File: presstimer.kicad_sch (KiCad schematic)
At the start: 31 parts, among them J1 Screw_Terminal_01x02, Q1 NPN, Q2 NPN, SW1 SW_Push, SW2 SW_Push, U1 AP7361C-33ER, U2 ESP32-S3-WROOM-1

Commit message: parts assigned, footprints checked
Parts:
- R1, R2: LCSC (none) -> C99782
- R13: LCSC (none) -> C105881
- R14: LCSC (none) -> C116677
- R3: LCSC (none) -> C22548
- R4: LCSC (none) -> C17477
- SW1, SW2: LCSC (none) -> C720477
- U1: LCSC (none) -> C3743528
- U2: LCSC (none) -> C2913202
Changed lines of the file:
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@@
 			)
 		)
+		(property "LCSC" "C99782"
+			(at 68.58 134.62 0)
+			(hide yes)
+			(show_name no)
+			(do_not_autoplace no)
+			(effects
+				(font
+					(size 1.27 1.27)
+				)
+			)
+		)
 		(pin "2"
 		)
@@
 		(property "LCSC" "C77049"
 			(at 186.69 63.4999 0)
+			(hide yes)
+			(show_name no)
+			(do_not_autoplace no)
 			(effects
 				(font
 					(size 1.27 1.27)
 				)
-				(hide yes)
 			)
 		)
@@
 		(property "LCSC" "C28323"
 			(at 54.61 33.0199 0)
+			(hide yes)
+			(show_name no)
+			(do_not_autoplace no)
 			(effects
 				(font
 					(size 1.27 1.27)
 				)
-				(hide yes)
 			)
 		)
@@
 			)
 		)
+		(property "LCSC" "C720477"
+			(at 161.29 125.73 0)
+			(hide yes)
+			(show_name no)
+			(do_not_autoplace no)
+			(effects
+				(font
+					(size 1.27 1.27)
+				)
+			)
+		)
 		(pin "2"
 		)
@@
 			)
 		)
+		(property "LCSC" "C105881"
+			(at 137.16 163.83 0)
+			(hide yes)
+			(show_name no)
+			(do_not_autoplace no)
+			(effects
+				(font
+					(size 1.27 1.27)
+				)
+			)
+		)
 		(pin "2"
 		)
@@
 		(property "LCSC" "C28326707"
 			(at 44.45 20.32 0)
+			(hide yes)
+			(show_name no)
+			(do_not_autoplace no)
 			(effects
 				(font
 					(size 1.27 1.27)
 				)
-				(hide yes)
 			)
 		)
@@
 			)
 		)
+		(property "LCSC" "C720477"
+			(at 124.46 125.73 0)
+			(hide yes)
+			(show_name no)
+			(do_not_autoplace no)
+			(effects
+				(font
+					(size 1.27 1.27)
+				)
+			)
+		)
 		(pin "2"
 		)
@@
 			)
 		)
+		(property "LCSC" "C22548"
+			(at 95.25 33.0199 0)
+			(hide yes)
+			(show_name no)
+			(do_not_autoplace no)
+			(effects
+				(font
+					(size 1.27 1.27)
+				)
+			)
+		)
 		(pin "2"
 		)
@@
 			)
 		)
+		(property "LCSC" "C17477"
+			(at 124.46 163.83 0)
+			(hide yes)
+			(show_name no)
+			(do_not_autoplace no)
+			(effects
+				(font
+					(size 1.27 1.27)
+				)
+			)
+		)
 		(pin "2"
 		)
@@
 			)
 		)
+		(property "LCSC" "C2913202"
+			(at 228.2033 54.61 0)
+			(hide yes)
+			(show_name no)
+			(do_not_autoplace no)
+			(effects
+				(font
+					(size 1.27 1.27)
+				)
+			)
+		)
 		(pin "7"
 		)
@@
 			)
 		)
+		(property "LCSC" "C99782"
+			(at 68.58 152.4 0)
+			(hide yes)
+			(show_name no)
+			(do_not_autoplace no)
+			(effects
+				(font
+					(size 1.27 1.27)
+				)
+			)
+		)
 		(pin "2"
 		)
@@
 			)
 		)
+		(property "LCSC" "C116677"
+			(at 185.42 52.0699 0)
+			(hide yes)
+			(show_name no)
+			(do_not_autoplace no)
+			(effects
+				(font
+					(size 1.27 1.27)
+				)
+			)
+		)
 		(pin "2"
 		)
@@
 		(property "LCSC" "C2922787"
 			(at 165.1 163.7598 0)
+			(hide yes)
+			(show_name no)
+			(do_not_autoplace no)
 			(effects
 				(font
 					(size 1.27 1.27)
 				)
-				(hide yes)
 			)
 		)
@@
 		(property "LCSC" "C237493"
 			(at 203.2 38.0999 0)
+			(hide yes)
+			(show_name no)
+			(do_not_autoplace no)
 			(effects
 				(font
 					(size 1.27 1.27)
 				)
-				(hide yes)
 			)
 		)
@@
 		(property "LCSC" "C84256"
 			(at 87.9475 19.05 0)
+			(hide yes)
+			(show_name no)
+			(do_not_autoplace no)
 			(effects
 				(font
 					(size 1.27 1.27)
 				)
-				(hide yes)
 			)
 		)
@@
 		(property "LCSC" "C28323"
 			(at 82.55 33.0199 0)
+			(hide yes)
+			(show_name no)
+			(do_not_autoplace no)
 			(effects
 				(font
 					(size 1.27 1.27)
 				)
-				(hide yes)
 			)
 		)
@@
 		(property "LCSC" "C5632695"
 			(at 26.67 20.32 0)
+			(hide yes)
+			(show_name no)
+			(do_not_autoplace no)
 			(effects
 				(font
 					(size 1.27 1.27)
 				)
-				(hide yes)
 			)
 		)
@@
 			)
 		)
+		(property "LCSC" "C3743528"
+			(at 68.58 20.32 0)
+			(hide yes)
+			(show_name no)
+			(do_not_autoplace no)
+			(effects
+				(font
+					(size 1.27 1.27)
+				)
+			)
+		)
 		(pin "3"
 		)
@@
 		(property "LCSC" "C77055"
 			(at 218.44 38.0999 0)
+			(hide yes)
+			(show_name no)
+			(do_not_autoplace no)
 			(effects
 				(font
 					(size 1.27 1.27)
 				)
-				(hide yes)
 			)
 		)

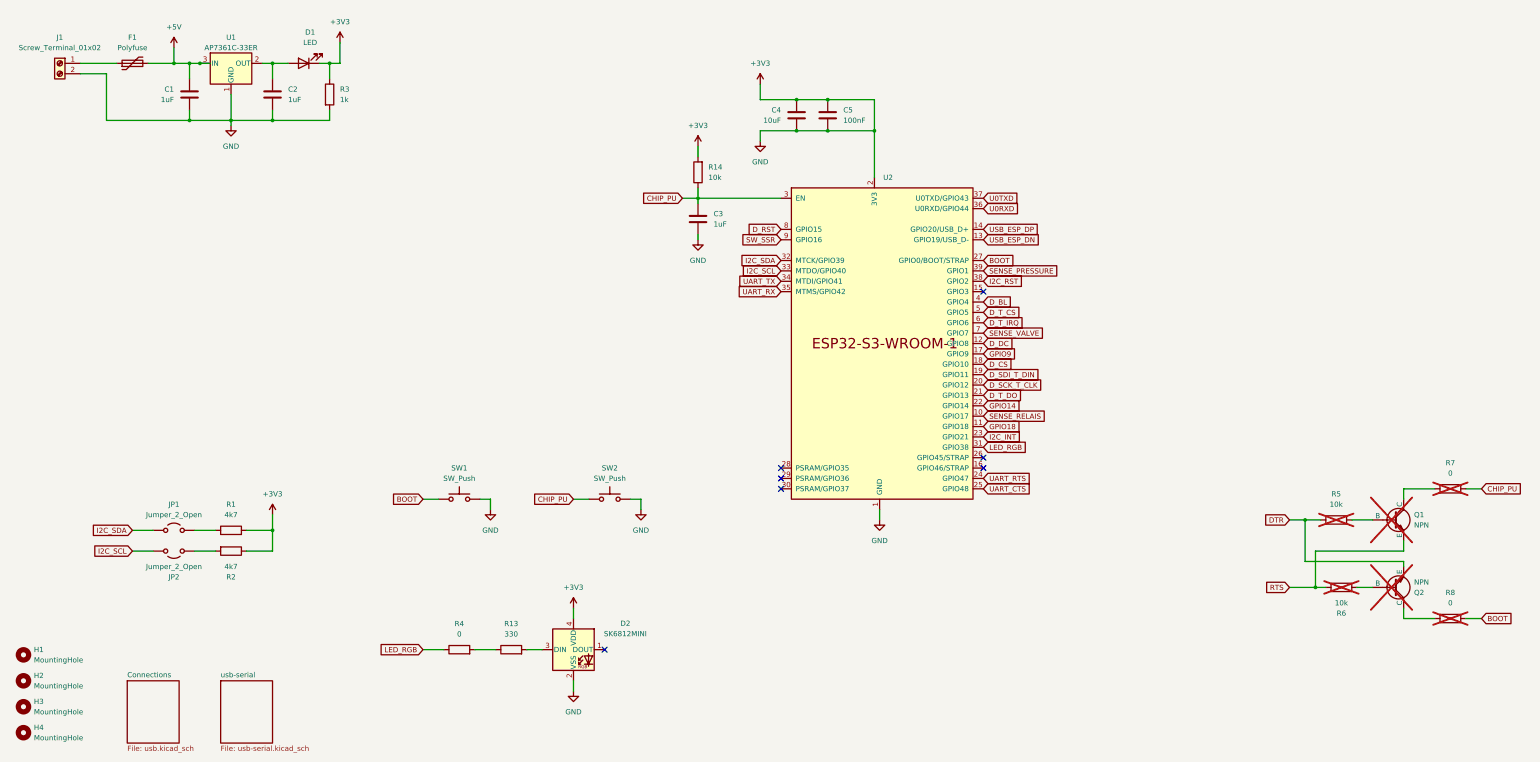
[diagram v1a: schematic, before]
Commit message: started pcb layout
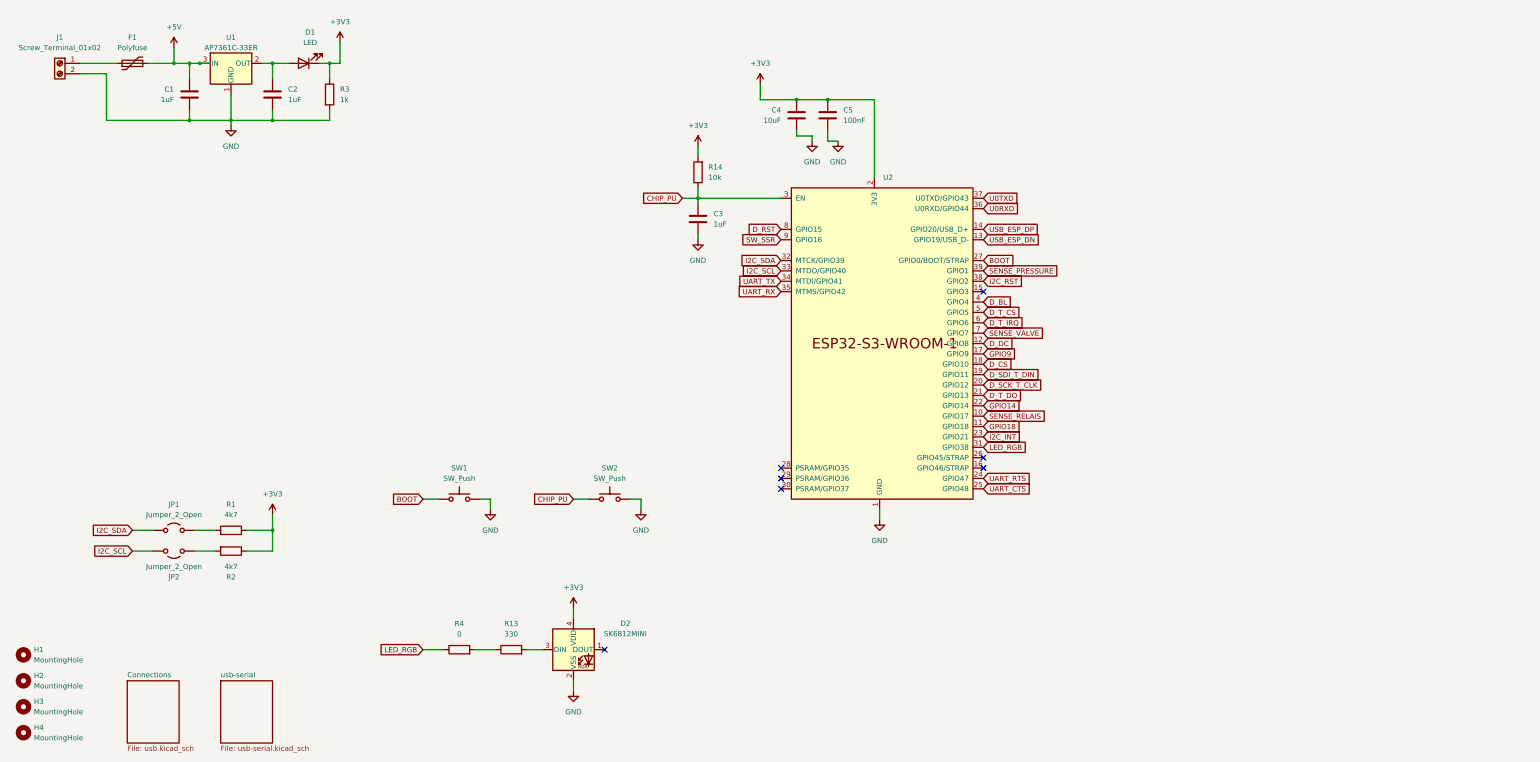
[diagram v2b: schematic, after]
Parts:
- removed Q1, Q2: NPN, symbol Simulation_SPICE:NPN
- removed R5, R6: 10k, symbol Device:R
- removed R7, R8: 0, symbol Device:R
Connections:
- net +3V3: no longer C1.2, C2.2, C3.2, C4.2, C5.2, D2.2 (VSS), J1.2 (Pin_2), R3.2, SW1.2, SW2.2, U1.1 (GND), U2.1 (GND)
- new net GND: C1.2, C2.2, C3.2, C4.2, C5.2, D2.2 (VSS), J1.2 (Pin_2), R3.2, SW1.2, SW2.2, U1.1 (GND), U2.1 (GND)

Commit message: pcb layout v0.0.2
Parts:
- removed JP1, JP2: Jumper_2_Open, Connector_PinHeader_2.54mm:PinHeader_1x02_P2.54mm_Vertical, symbol Jumper:Jumper_2_Open
- added R5, R6: 0, PCM_JLCPCB:R_0603, symbol Device:R
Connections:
- net I2C_SCL: now also R6.2
- net I2C_SDA: now also R5.1
- net at R1.1: now also R5.2
- net at R2.2: now also R6.1
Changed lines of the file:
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@@
 	(wire
 		(pts
-			(xy 59.69 146.05) (xy 64.77 146.05)
-		)
-		(stroke
-			(width 0)
-			(type default)
-		)
-	)
-	(wire
-		(pts
 			(xy 182.88 46.99) (xy 182.88 49.53)
 		)
@@
 	(wire
 		(pts
-			(xy 59.69 140.97) (xy 64.77 140.97)
-		)
-		(stroke
-			(width 0)
-			(type default)
-		)
-	)
-	(wire
-		(pts
 			(xy 68.58 40.64) (xy 68.58 41.91)
 		)
@@
 	(wire
 		(pts
+			(xy 58.42 146.05) (xy 64.77 146.05)
+		)
+		(stroke
+			(width 0)
+			(type default)
+		)
+	)
+	(wire
+		(pts
 			(xy 31.75 29.21) (xy 38.1 29.21)
 		)
@@
 	(wire
 		(pts
-			(xy 44.45 146.05) (xy 49.53 146.05)
+			(xy 44.45 146.05) (xy 50.8 146.05)
 		)
 		(stroke
@@
 	(wire
 		(pts
+			(xy 58.42 140.97) (xy 64.77 140.97)
+		)
+		(stroke
+			(width 0)
+			(type default)
+		)
+	)
+	(wire
+		(pts
 			(xy 58.42 26.67) (xy 60.96 26.67)
 		)
@@
 	(wire
 		(pts
-			(xy 44.45 140.97) (xy 49.53 140.97)
+			(xy 44.45 140.97) (xy 50.8 140.97)
 		)
 		(stroke
@@
 	(symbol
 		(lib_id "Device:R")
+		(at 54.61 146.05 270)
+		(unit 1)
+		(body_style 1)
+		(exclude_from_sim no)
+		(in_bom yes)
+		(on_board yes)
+		(in_pos_files yes)
+		(dnp no)
+		(property "Reference" "R6"
+			(at 54.61 152.4 90)
+			(show_name no)
+			(do_not_autoplace no)
+			(effects
+				(font
+					(size 1.27 1.27)
+				)
+			)
+		)
+		(property "Value" "0"
+			(at 54.61 149.86 90)
+			(show_name no)
+			(do_not_autoplace no)
+			(effects
+				(font
+					(size 1.27 1.27)
+				)
+			)
+		)
+		(property "Footprint" "PCM_JLCPCB:R_0603"
+			(at 54.61 144.272 90)
+			(hide yes)
+			(show_name no)
+			(do_not_autoplace no)
+			(effects
+				(font
+					(size 1.27 1.27)
+				)
+			)
+		)
+		(property "Datasheet" ""
+			(at 54.61 146.05 0)
+			(hide yes)
+			(show_name no)
+			(do_not_autoplace no)
+			(effects
+				(font
+					(size 1.27 1.27)
+				)
+			)
+		)
+		(property "Description" "Resistor"
+			(at 54.61 146.05 0)
+			(hide yes)
+			(show_name no)
+			(do_not_autoplace no)
+			(effects
+				(font
+					(size 1.27 1.27)
+				)
+			)
+		)
+		(property "LCSC" "C21189"
+			(at 54.61 152.4 0)
+			(effects
+				(font
+					(size 1.27 1.27)
+				)
+				(hide yes)
+			)
+		)
+		(pin "1"
+		)
+		(pin "2"
+		)
+		(instances
+			(project "presstimer"
+				(path "/63494a82-20b5-470b-977d-6a82bfa70174"
+					(reference "R6")
+					(unit 1)
+				)
+			)
+		)
+	)
+	(symbol
+		(lib_id "Device:R")
 		(at 68.58 140.97 90)
 		(unit 1)
@@
 	)
 	(symbol
-		(lib_id "Jumper:Jumper_2_Open")
-		(at 54.61 146.05 0)
-		(mirror x)
+		(lib_id "Device:R")
+		(at 54.61 140.97 90)
 		(unit 1)
 		(body_style 1)
 		(exclude_from_sim no)
-		(in_bom no)
+		(in_bom yes)
 		(on_board yes)
 		(in_pos_files yes)
 		(dnp no)
-		(property "Reference" "JP2"
-			(at 54.61 152.4 0)
+		(fields_autoplaced yes)
+		(property "Reference" "R5"
+			(at 54.61 134.62 90)
 			(show_name no)
 			(do_not_autoplace no)
@@
 			)
 		)
-		(property "Value" "Jumper_2_Open"
-			(at 54.61 149.86 0)
+		(property "Value" "0"
+			(at 54.61 137.16 90)
 			(show_name no)
 			(do_not_autoplace no)
@@
 			)
 		)
-		(property "Footprint" "Connector_PinHeader_2.54mm:PinHeader_1x02_P2.54mm_Vertical"
-			(at 54.61 146.05 0)
+		(property "Footprint" "PCM_JLCPCB:R_0603"
+			(at 54.61 142.748 90)
 			(hide yes)
 			(show_name no)
@@
 		)
 		(property "Datasheet" ""
-			(at 54.61 146.05 0)
+			(at 54.61 140.97 0)
 			(hide yes)
 			(show_name no)
@@
 			)
 		)
-		(property "Description" "Jumper, 2-pole, open"
-			(at 54.61 146.05 0)
+		(property "Description" "Resistor"
+			(at 54.61 140.97 0)
 			(hide yes)
 			(show_name no)
@@
 			)
 		)
-		(pin "2"
+		(property "LCSC" "C21189"
+			(at 54.61 134.62 0)
+			(effects
+				(font
+					(size 1.27 1.27)
+				)
+				(hide yes)
+			)
 		)
 		(pin "1"
 		)
+		(pin "2"
+		)
 		(instances
 			(project "presstimer"
 				(path "/63494a82-20b5-470b-977d-6a82bfa70174"
-					(reference "JP2")
+					(reference "R5")
 					(unit 1)
 				)
@@
 					(unit 1)
 				)
-			)
-		)
-	)
-	(symbol
-		(lib_id "Jumper:Jumper_2_Open")
-		(at 54.61 140.97 0)
-		(unit 1)
-		(body_style 1)
-		(exclude_from_sim no)
-		(in_bom no)
-		(on_board yes)
-		(in_pos_files yes)
-		(dnp no)
-		(fields_autoplaced yes)
-		(property "Reference" "JP1"
-			(at 54.61 134.62 0)
-			(show_name no)
-			(do_not_autoplace no)
-			(effects
-				(font
-					(size 1.27 1.27)
-				)
-			)
-		)
-		(property "Value" "Jumper_2_Open"
-			(at 54.61 137.16 0)
-			(show_name no)
-			(do_not_autoplace no)
-			(effects
-				(font
-					(size 1.27 1.27)
-				)
-			)
-		)
-		(property "Footprint" "Connector_PinHeader_2.54mm:PinHeader_1x02_P2.54mm_Vertical"
-			(at 54.61 140.97 0)
-			(hide yes)
-			(show_name no)
-			(do_not_autoplace no)
-			(effects
-				(font
-					(size 1.27 1.27)
-				)
-			)
-		)
-		(property "Datasheet" ""
-			(at 54.61 140.97 0)
-			(hide yes)
-			(show_name no)
-			(do_not_autoplace no)
-			(effects
-				(font
-					(size 1.27 1.27)
-				)
-			)
-		)
-		(property "Description" "Jumper, 2-pole, open"
-			(at 54.61 140.97 0)
-			(hide yes)
-			(show_name no)
-			(do_not_autoplace no)
-			(effects
-				(font
-					(size 1.27 1.27)
-				)
-			)
-		)
-		(pin "2"
-		)
-		(pin "1"
-		)
-		(instances
-			(project "presstimer"
-				(path "/63494a82-20b5-470b-977d-6a82bfa70174"
-					(reference "JP1")
-					(unit 1)
-				)

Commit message: routing finished v0.1.0
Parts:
- added TP1, TP2: TestPoint, TestPoint:TestPoint_Pad_D1.5mm, symbol Connector:TestPoint
- added TP3: TestPoint, TestPoint:TestPoint_Pad_1.5x1.5mm, symbol Connector:TestPoint
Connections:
- net OUT is gone; now on an unnamed net: U1.4 (OUT)
- net +3V3: now also TP2.1
- net GND: now also U2.41 (GND), TP3.1
- net at F1.1, J1.1 (Pin_1): now also TP1.1

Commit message: board finished v1.0
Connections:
- net GND: now also U2.40 (GND)
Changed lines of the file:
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@@
+	(wire
+		(pts
+			(xy 248.92 135.89) (xy 248.92 138.43)
+		)
+		(stroke
+			(width 0)
+			(type default)
+		)
+	)
 	(wire
 		(pts
@@
 	(symbol
 		(lib_id "power:GND")
-		(at 232.41 135.89 0)
+		(at 248.92 138.43 0)
 		(unit 1)
 		(body_style 1)
@@
 		(fields_autoplaced yes)
 		(property "Reference" "#PWR017"
-			(at 232.41 142.24 0)
+			(at 248.92 144.78 0)
 			(hide yes)
 			(show_name no)
@@
 		)
 		(property "Value" "GND"
-			(at 232.41 140.97 0)
+			(at 248.92 143.51 0)
 			(show_name no)
 			(do_not_autoplace no)
@@
 		)
 		(property "Footprint" ""
-			(at 232.41 135.89 0)
+			(at 248.92 138.43 0)
 			(hide yes)
 			(show_name no)
@@
 		)
 		(property "Datasheet" ""
-			(at 232.41 135.89 0)
+			(at 248.92 138.43 0)
 			(hide yes)
 			(show_name no)
@@
 		)
 		(property "Description" "Power symbol creates a global label with name \"GND\" , ground"
-			(at 232.41 135.89 0)
-			(hide yes)
-			(show_name no)
+			(at 248.92 138.43 0)
+			(hide yes)
+			(show_name no)
